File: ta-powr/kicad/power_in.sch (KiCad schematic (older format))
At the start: 29 parts, among them U1 SPV1040, U3 TLV8544DT, U4 ADS1115-Q1

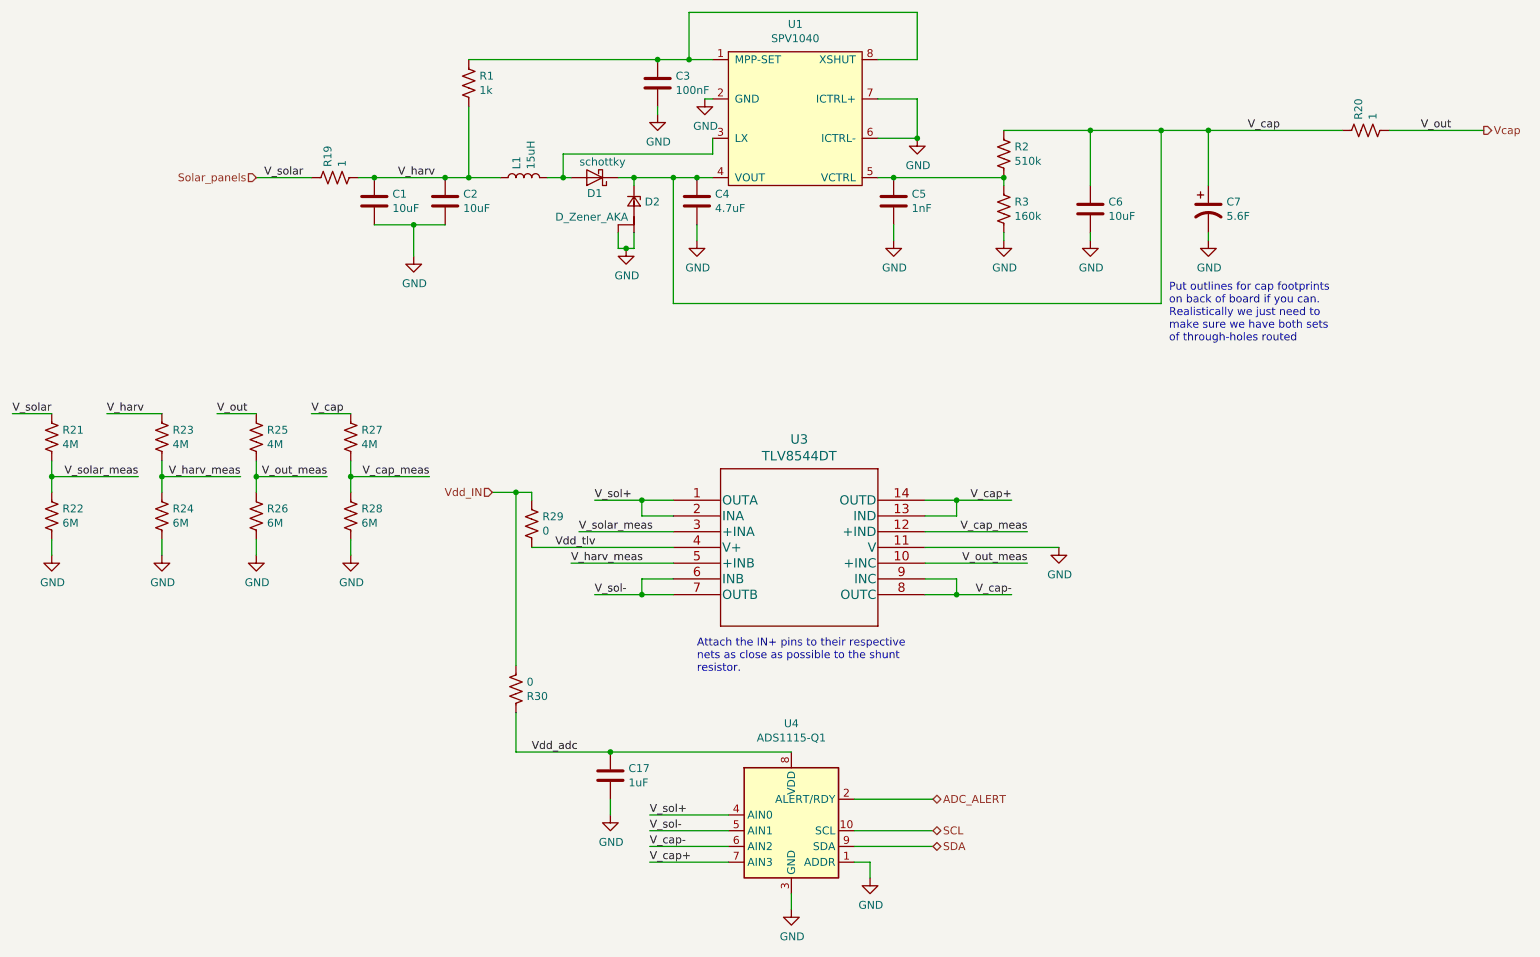
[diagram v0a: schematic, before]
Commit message: fixes to power board after testing
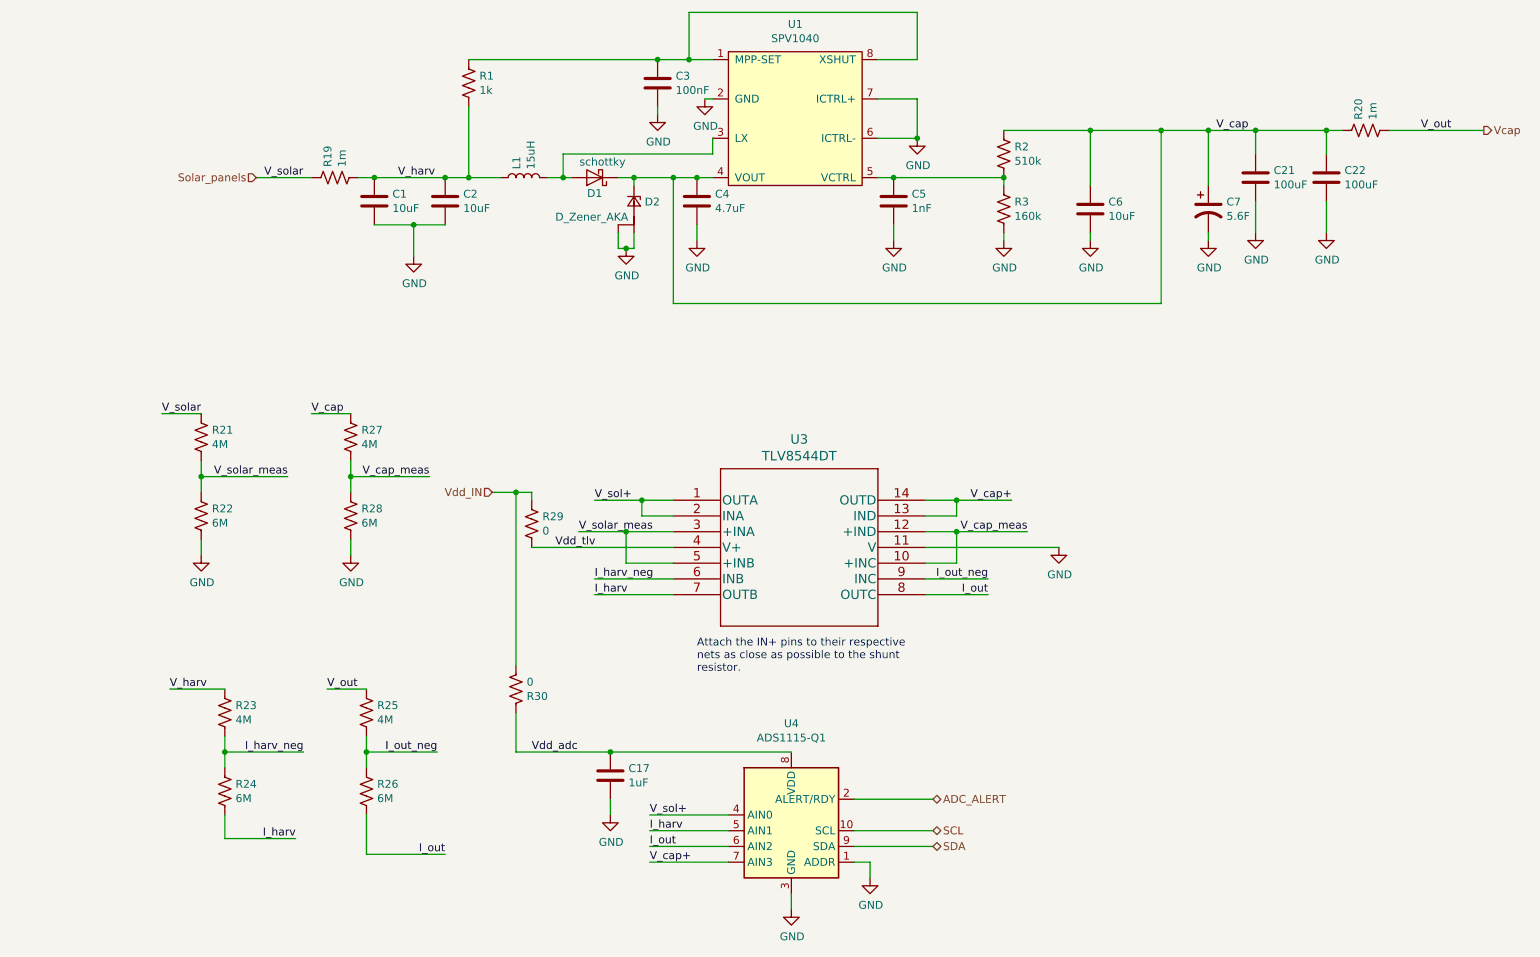
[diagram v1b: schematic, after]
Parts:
- added C21, C22: 100uF, Capacitor_SMD:C_1210_3225Metric, symbol Device:C
- R19, R20: value 1 -> 1m; footprint Resistor_SMD:R_2512_6332Metric -> Resistor_SMD:R_1206_3216Metric; Manufacturer Part Number CRCW25121R00FKEG -> WSLP12061L000FEA; Vendor Digikey -> Mouser; Vendor Part Number 541-1.00AAFCT-ND -> 71-WSLP12061L000FEA
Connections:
- net GND: now also C21.2, C22.2; no longer R24.2, R26.2
- net V_cap: now also C21.1, C22.1
- net V_cap_meas: now also U3.10 (+INC)
- net V_solar_meas: now also U3.5 (+INB)
- net V_cap- renamed I_out
- net I_out: now also R26.2; no longer U3.9 (INC)
- net V_harv_meas renamed I_harv_neg
- net I_harv_neg: now also U3.6 (INB); no longer U3.5 (+INB)
- net V_out_meas renamed I_out_neg
- net I_out_neg: now also U3.9 (INC); no longer U3.10 (+INC)
- net V_sol- renamed I_harv
- net I_harv: now also R24.2; no longer U3.6 (INB)
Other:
- note removed: "Put outlines for cap footprints \non back of board if you can. \nRealistically we just need to \nmake sure we have both sets\nof through-holes routed"
- moved on the sheet: R21, R22, R23, R25, R26
